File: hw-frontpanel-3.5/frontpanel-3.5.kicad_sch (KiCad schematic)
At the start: 34 parts, among them J1 FRONT_PANEL, J2 QWIIC, J3 Conn_01x02_Pin, J5 OLED_SH1107, J6 Conn_01x12_MountingPin, SW1 SW_Push, SW2 SW_Push, SW3 SW_Push, SW4 SW_Push, U1 MT3540, U2 LM809, U3 TCA9535PWR

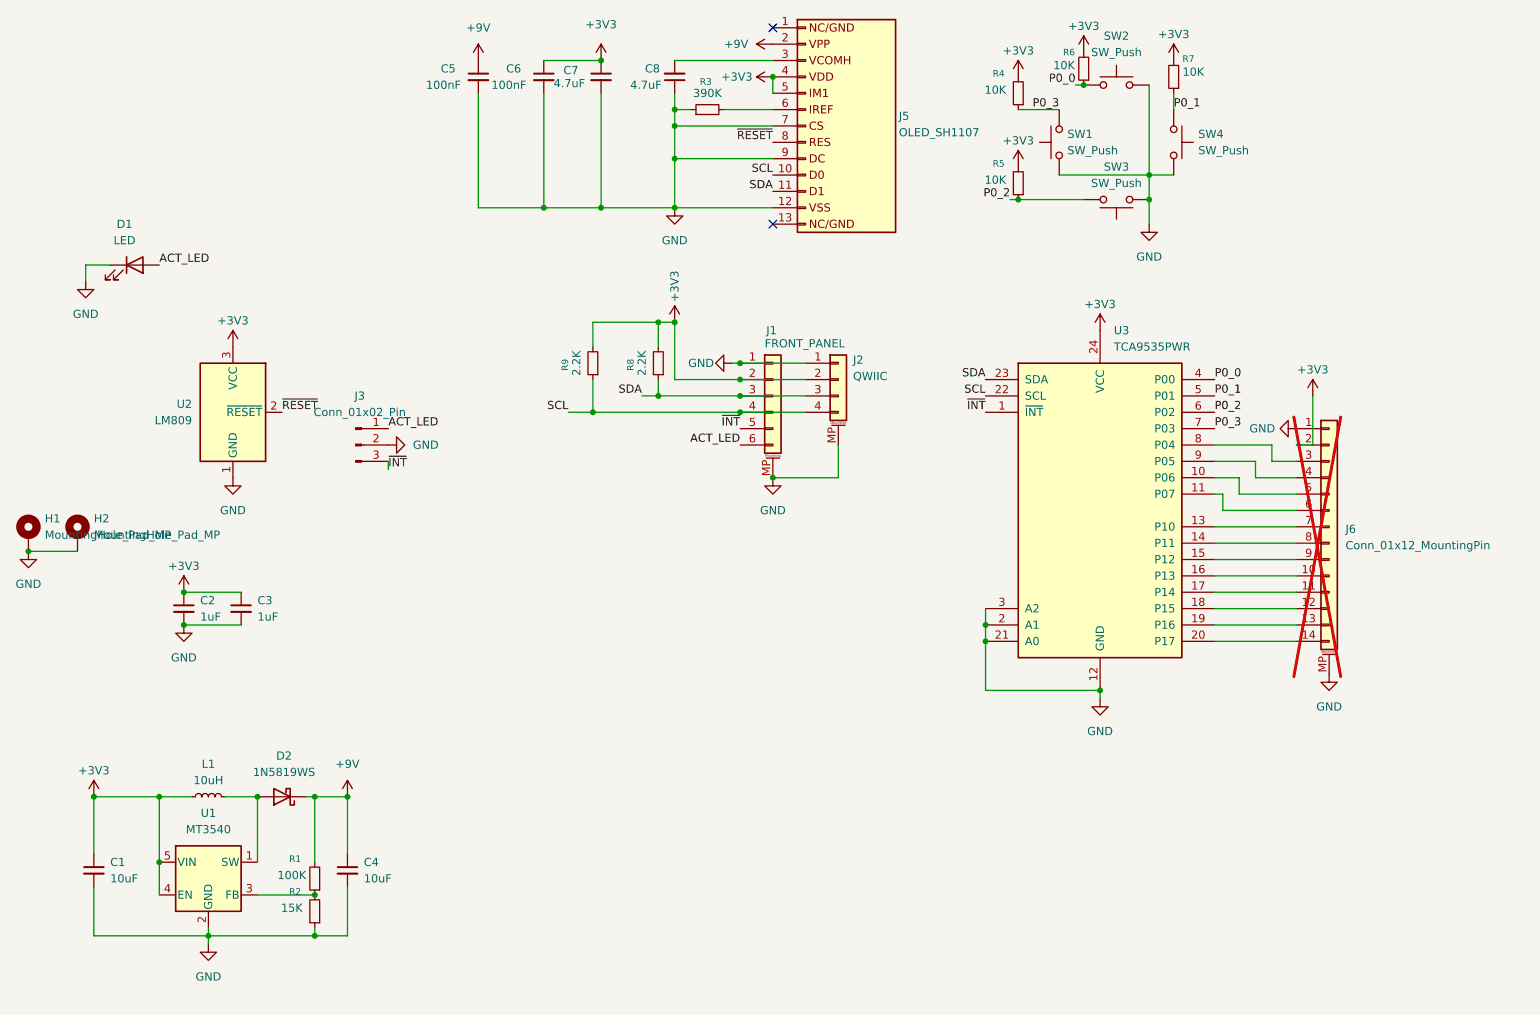
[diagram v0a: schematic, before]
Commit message: Front panel board fabbed at JLCPCB 2025-09-17
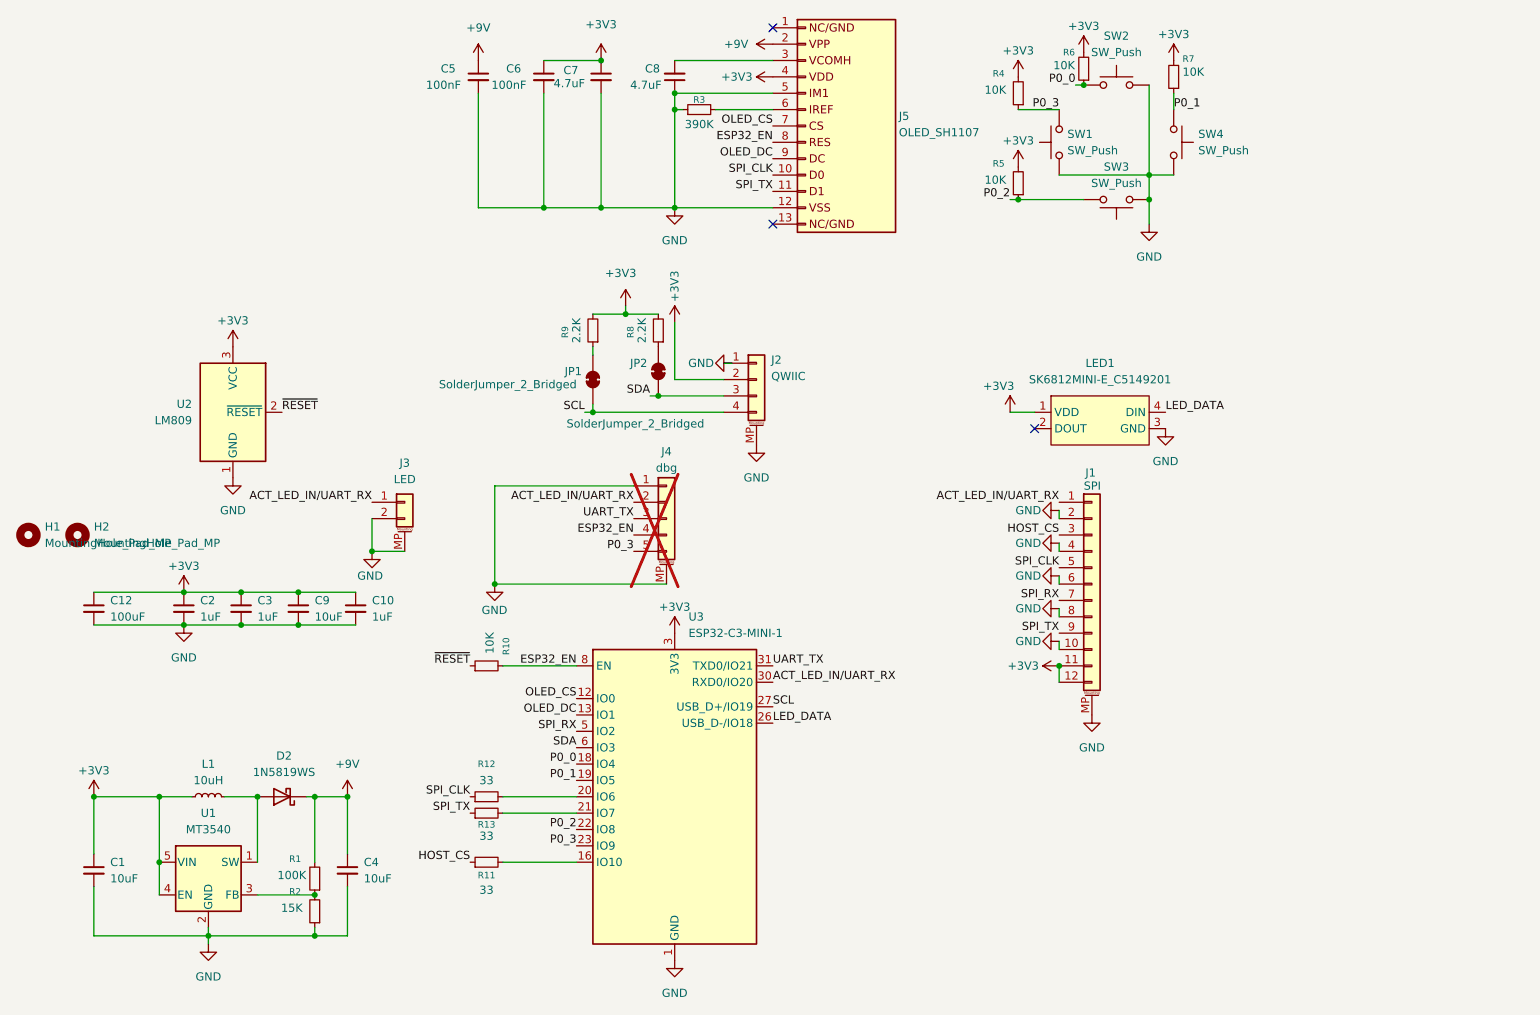
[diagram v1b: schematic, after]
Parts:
- removed D1: LED, LED_SMD:LED_1206_3216Metric_ReverseMount_Hole1.8x2.4mm, symbol Device:LED
- removed J6: Conn_01x12_MountingPin, Connector_JST:JST_SH_BM14B-SRSS-TB_1x14-1MP_P1.00mm_Vertical, symbol Connector_Generic_MountingPin:Conn_01x14_MountingPin
- removed U3: TCA9535PWR, Package_SO:TSSOP-24_4.4x7.8mm_P0.65mm, symbol Interface_Expansion:TCA9535PWR
- added C10: 1uF, Capacitor_SMD:C_0402_1005Metric, symbol Device:C_Small
- added C12: 100uF, Capacitor_SMD:C_1206_3216Metric, symbol Device:C_Small
- added C9: 10uF, Capacitor_SMD:C_0603_1608Metric, symbol Device:C_Small
- added J4: dbg, Connector_JST:JST_SH_BM05B-SRSS-TB_1x05-1MP_P1.00mm_Vertical, symbol Connector_Generic_MountingPin:Conn_01x05_MountingPin
- added JP1, JP2: SolderJumper_2_Bridged, Jumper:SolderJumper-2_P1.3mm_Bridged_RoundedPad1.0x1.5mm, symbol Jumper:SolderJumper_2_Bridged
- added LED1: SK6812MINI-E_C5149201, frontpanel:LED-SMD_L3.2-W2.8-LS5.9_SK6812MINI-E, symbol frontpanel:SK6812MINI-E_C5149201
- added R10: 10K, Resistor_SMD:R_0402_1005Metric, symbol Device:R_Small
- added R11, R12, R13: 33, Resistor_SMD:R_0402_1005Metric, symbol Device:R_Small
- added U3: ESP32-C3-MINI-1, RF_Module:ESP32-C6-MINI-1, symbol frontpanel:ESP32-C3-MINI-1
- C2, C3, C5, C6: footprint Capacitor_SMD:C_0603_1608Metric -> Capacitor_SMD:C_0402_1005Metric
- H1, H2: footprint MountingHole:MountingHole_2.2mm_M2_Pad -> MountingHole:MountingHole_2.2mm_M2; symbol Mechanical:MountingHole_Pad -> Mechanical:MountingHole
- J1: value FRONT_PANEL -> SPI; footprint Connector_JST:JST_SH_BM06B-SRSS-TB_1x06-1MP_P1.00mm_Vertical -> frontpanel:FPC-SMD_12P-L11.5-W2.0-P0.50; symbol Connector_Generic_MountingPin:Conn_01x06_MountingPin -> Connector_Generic_MountingPin:Conn_01x12_MountingPin
- J3: value Conn_01x02_Pin -> LED; footprint Connector_PinHeader_2.54mm:PinHeader_1x03_P2.54mm_Vertical_SMD_Pin1Left -> Connector_JST:JST_SH_BM02B-SRSS-TB_1x02-1MP_P1.00mm_Vertical; symbol Connector:Conn_01x03_Pin -> Connector_Generic_MountingPin:Conn_01x02_MountingPin
- R1, R2, R3, R4, R5, R6, R7, R8, R9: footprint Resistor_SMD:R_0603_1608Metric -> Resistor_SMD:R_0402_1005Metric
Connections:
- net +3V3: now also J1.11 (Pin_11), J1.12 (Pin_12), C10.1, C12.1, C9.1, LED1.1 (VDD), U3.3 (3V3); no longer J1.2 (Pin_2), J5.5 (Pin_5)
- net GND: now also J1.10 (Pin_10), J1.2 (Pin_2), J1.4 (Pin_4), J1.6 (Pin_6), J1.8 (Pin_8), J3.MP (MountPin), J5.5 (Pin_5), C10.2, C12.2, C9.2, J4.1 (Pin_1), J4.MP (MountPin), LED1.3 (GND), U3.1 (GND), U3.11 (GND), U3.14 (GND), U3.2 (GND), U3.36 (GND), U3.37 (GND), U3.38 (GND), U3.39 (GND), U3.40 (GND), U3.41 (GND), U3.42 (GND), U3.43 (GND), U3.44 (GND), U3.45 (GND), U3.46 (GND), U3.47 (GND), U3.48 (GND), U3.49 (GND), U3.50 (GND), U3.51 (GND), U3.52 (GND), U3.53 (GND); no longer H1.1, H2.1, J1.1 (Pin_1), J5.7 (Pin_7), J5.9 (Pin_9)
- net P0_0: now also U3.18 (IO4)
- net P0_1: now also U3.19 (IO5)
- net P0_2: now also U3.22 (IO8)
- net P0_3: now also J4.5 (Pin_5), U3.23 (IO9)
- net SCL: now also JP1.1 (A), U3.27 (USB_D+/IO19); no longer J1.4 (Pin_4), J5.10 (Pin_10), R9.1
- net SDA: now also JP2.1 (A), U3.6 (IO3); no longer J1.3 (Pin_3), J5.11 (Pin_11), R8.1
- net ~{RESET}: now also R10.1; no longer J5.8 (Pin_8)
- net ACT_LED renamed ACT_LED_IN/UART_RX
- net ACT_LED_IN/UART_RX: now also J1.1 (Pin_1), J4.2 (Pin_2), U3.30 (RXD0/IO20); no longer J1.6 (Pin_6)
- net ~{INT} renamed SPI_CLK
- net SPI_CLK: now also J5.10 (Pin_10), R12.1; no longer J3.3 (Pin_3)
- new net: JP1.2 (B), R9.1
- new net: JP2.2 (B), R8.1
- new net: R11.2, U3.16 (IO10)
- new net: R13.2, U3.21 (IO7)
- new net: R12.2, U3.20 (IO6)
- new net ESP32_EN: J4.4 (Pin_4), J5.8 (Pin_8), R10.2, U3.8 (EN)
- new net HOST_CS: J1.3 (Pin_3), R11.1
- new net LED_DATA: LED1.4 (DIN), U3.26 (USB_D-/IO18)
- new net OLED_CS: J5.7 (Pin_7), U3.12 (IO0)
- new net OLED_DC: J5.9 (Pin_9), U3.13 (IO1)
- new net SPI_RX: J1.7 (Pin_7), U3.5 (IO2)
- new net SPI_TX: J1.9 (Pin_9), J5.11 (Pin_11), R13.1
- new net UART_TX: J4.3 (Pin_3), U3.31 (TXD0/IO21)
- no-connect marks 2 -> 3
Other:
- moved on the sheet: J2, R3, R8, R9

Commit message: Use RC for ESP32 reset, power on reset for OLED
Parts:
- added C11: 1uF, Capacitor_SMD:C_0402_1005Metric, symbol Device:C_Small
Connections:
- net +3V3: now also R10.2
- net ESP32_EN: now also R10.1, C11.1; no longer J5.8 (Pin_8), R10.2
- net GND: now also C11.2
- net ~{RESET}: now also J5.8 (Pin_8); no longer R10.1
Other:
- moved on the sheet: J4, R10

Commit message: Provisional v1.0.0 hardware
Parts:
- removed J4: dbg, Connector_JST:JST_SH_BM05B-SRSS-TB_1x05-1MP_P1.00mm_Vertical, symbol Connector_Generic_MountingPin:Conn_01x05_MountingPin
- added J4: TC2030, Connector:Tag-Connect_TC2030-IDC-NL_2x03_P1.27mm_Vertical, symbol Connector:TC2030
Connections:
- net +3V3: now also J4.2
- net ACT_LED_IN/UART_RX: now also J4.5
- net ESP32_EN: now also J4.1
- net GND: now also J4.4
- net P0_3: now also J4.6
- net UART_TX: now also J4.3
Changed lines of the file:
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@@
 	)
 	(junction
-		(at 92.71 115.57)
-		(diameter 0)
-		(color 0 0 0 0)
-	)
-	(junction
 		(at 60.96 170.18)
 		(diameter 0)
@@
 	(wire
 		(pts
-			(xy 92.71 115.57) (xy 119.38 115.57)
-		)
-		(stroke
-			(width 0)
-			(type default)
-		)
-	)
-	(wire
-		(pts
 			(xy 116.84 34.29) (xy 132.08 34.29)
 		)
@@
 	(wire
 		(pts
-			(xy 92.71 100.33) (xy 114.3 100.33)
-		)
-		(stroke
-			(width 0)
-			(type default)
-		)
-	)
-	(wire
-		(pts
 			(xy 116.84 39.37) (xy 132.08 39.37)
 		)
@@
 	(wire
 		(pts
-			(xy 92.71 100.33) (xy 92.71 115.57)
+			(xy 144.78 104.14) (xy 144.78 105.41)
 		)
 		(stroke
@@
 	(wire
 		(pts
+			(xy 144.78 106.68) (xy 144.78 107.95)
+		)
+		(stroke
+			(width 0)
+			(type default)
+		)
+	)
+	(wire
+		(pts
 			(xy 168.91 88.9) (xy 172.72 88.9)
 		)
@@
 	)
 	(label "ACT_LED_IN{slash}UART_RX"
-		(at 114.3 102.87 180)
+		(at 132.08 110.49 180)
 		(effects
 			(font
@@
 	)
 	(label "P0_3"
-		(at 114.3 110.49 180)
+		(at 144.78 110.49 0)
 		(effects
 			(font
 				(size 1.27 1.27)
 			)
-			(justify right bottom)
+			(justify left bottom)
 		)
 	)
@@
 	)
 	(label "UART_TX"
-		(at 114.3 105.41 180)
+		(at 132.08 107.95 180)
 		(effects
 			(font
@@
 	)
 	(label "ESP32_EN"
-		(at 114.3 107.95 180)
+		(at 132.08 105.41 180)
 		(effects
 			(font
@@
 	)
 	(symbol
-		(lib_id "Connector_Generic_MountingPin:Conn_01x05_MountingPin")
-		(at 119.38 105.41 0)
-		(unit 1)
-		(exclude_from_sim no)
-		(in_bom yes)
-		(on_board yes)
-		(dnp yes)
-		(property "Reference" "J4"
-			(at 119.38 94.996 0)
-			(effects
-				(font
-					(size 1.27 1.27)
-				)
-			)
-		)
-		(property "Value" "dbg"
-			(at 119.38 97.536 0)
-			(effects
-				(font
-					(size 1.27 1.27)
-				)
-			)
-		)
-		(property "Footprint" "Connector_JST:JST_SH_BM05B-SRSS-TB_1x05-1MP_P1.00mm_Vertical"
-			(at 119.38 105.41 0)
-			(effects
-				(font
-					(size 1.27 1.27)
-				)
-				(hide yes)
-			)
-		)
-		(property "Datasheet" "~"
-			(at 119.38 105.41 0)
-			(effects
-				(font
-					(size 1.27 1.27)
-				)
-				(hide yes)
-			)
-		)
-		(property "Description" "Generic connectable mounting pin connector, single row, 01x05, script generated (kicad-library-utils/schlib/autogen/connector/)"
-			(at 119.38 105.41 0)
-			(effects
-				(font
-					(size 1.27 1.27)
-				)
-				(hide yes)
-			)
-		)
-		(property "LCSC" "C22438427"
-			(at 119.38 105.41 0)
-			(effects
-				(font
-					(size 1.27 1.27)
-				)
-				(hide yes)
-			)
-		)
-		(pin "2"
-		)
-		(pin "1"
-		)
-		(pin "3"
-		)
-		(pin "MP"
-		)
-		(pin "5"
-		)
-		(pin "4"
-		)
-		(instances
-			(project "frontpanel-3.5"
-				(path "/c6faebfb-76d3-4c2f-8f32-d834e013b78c"
-					(reference "J4")
-					(unit 1)
-				)
-			)
-		)
-	)
-	(symbol
 		(lib_id "Device:R_Small")
 		(at 87.63 151.13 90)
@@
 	)
 	(symbol
+		(lib_id "power:+3V3")
+		(at 144.78 104.14 270)
+		(unit 1)
+		(exclude_from_sim no)
+		(in_bom yes)
+		(on_board yes)
+		(dnp no)
+		(property "Reference" "#PWR037"
+			(at 140.97 104.14 0)
+			(effects
+				(font
+					(size 1.27 1.27)
+				)
+				(hide yes)
+			)
+		)
+		(property "Value" "+3V3"
+			(at 150.114 104.14 90)
+			(effects
+				(font
+					(size 1.27 1.27)
+				)
+			)
+		)
+		(property "Footprint" ""
+			(at 144.78 104.14 0)
+			(effects
+				(font
+					(size 1.27 1.27)
+				)
+				(hide yes)
+			)
+		)
+		(property "Datasheet" ""
+			(at 144.78 104.14 0)
+			(effects
+				(font
+					(size 1.27 1.27)
+				)
+				(hide yes)
+			)
+		)
+		(property "Description" "Power symbol creates a global label with name \"+3V3\""
+			(at 144.78 104.14 0)
+			(effects
+				(font
+					(size 1.27 1.27)
+				)
+				(hide yes)
+			)
+		)
+		(pin "1"
+		)
+		(instances
+			(project "frontpanel-3.5"
+				(path "/c6faebfb-76d3-4c2f-8f32-d834e013b78c"
+					(reference "#PWR037")
+					(unit 1)
+				)
+			)
+		)
+	)
+	(symbol
 		(lib_id "Device:C_Small")
 		(at 96.52 36.83 0)
@@
 	(symbol
 		(lib_id "power:GND")
-		(at 92.71 115.57 0)
-		(unit 1)
-		(exclude_from_sim no)
-		(in_bom yes)
-		(on_board yes)
-		(dnp no)
-		(property "Reference" "#PWR02"
-			(at 92.71 121.92 0)
-			(effects
-				(font
-					(size 1.27 1.27)
-				)
-				(hide yes)
-			)
-		)
-		(property "Value" "GND"
-			(at 90.678 119.634 0)
-			(effects
-				(font
-					(size 1.27 1.27)
-				)
-				(justify left)
-			)
-		)
-		(property "Footprint" ""
-			(at 92.71 115.57 0)
-			(effects
-				(font
-					(size 1.27 1.27)
-				)
-				(hide yes)
-			)
-		)
-		(property "Datasheet" ""
-			(at 92.71 115.57 0)
-			(effects
-				(font
-					(size 1.27 1.27)
-				)
-				(hide yes)
-			)
-		)
-		(property "Description" "Power symbol creates a global label with name \"GND\" , ground"
-			(at 92.71 115.57 0)
-			(effects
-				(font
-					(size 1.27 1.27)
-				)
-				(hide yes)
-			)
-		)
-		(pin "1"
-		)
-		(instances
-			(project "frontpanel-3.5"
-				(path "/c6faebfb-76d3-4c2f-8f32-d834e013b78c"
-					(reference "#PWR02")
-					(unit 1)
-				)
-			)
-		)
-	)
-	(symbol
-		(lib_id "power:GND")
 		(at 176.53 124.46 270)
 		(unit 1)
@@
 	)
 	(symbol
+		(lib_id "power:GND")
+		(at 144.78 106.68 90)
+		(unit 1)
+		(exclude_from_sim no)
+		(in_bom yes)
+		(on_board yes)
+		(dnp no)
+		(fields_autoplaced yes)
+		(property "Reference" "#PWR038"
+			(at 151.13 106.68 0)
+			(effects
+				(font
+					(size 1.27 1.27)
+				)
+				(hide yes)
+			)
+		)
+		(property "Value" "GND"
+			(at 148.59 106.6799 90)
+			(effects
+				(font
+					(size 1.27 1.27)
+				)
+				(justify right)
+			)
+		)
+		(property "Footprint" ""
+			(at 144.78 106.68 0)
+			(effects
+				(font
+					(size 1.27 1.27)
+				)
+				(hide yes)
+			)
+		)
+		(property "Datasheet" ""
+			(at 144.78 106.68 0)
+			(effects
+				(font
+					(size 1.27 1.27)
+				)
+				(hide yes)
+			)
+		)
+		(property "Description" "Power symbol creates a global label with name \"GND\" , ground"
+			(at 144.78 106.68 0)
+			(effects
+				(font
+					(size 1.27 1.27)
+				)
+				(hide yes)
+			)
+		)
+		(pin "1"
+		)
+		(instances
+			(project "frontpanel-3.5"
+				(path "/c6faebfb-76d3-4c2f-8f32-d834e013b78c"
+					(reference "#PWR038")
+					(unit 1)
+				)
+			)
+		)
+	)
+	(symbol
 		(lib_id "Device:C_Small")
 		(at 26.67 119.38 0)
@@
 					(unit 1)
 				)
+			)
+		)
+	)
+	(symbol
+		(lib_id "Connector:TC2030")
+		(at 137.16 107.95 0)
+		(unit 1)
+		(exclude_from_sim no)
+		(in_bom no)
+		(on_board yes)
+		(dnp no)
+		(fields_autoplaced yes)
+		(property "Reference" "J4"
+			(at 138.43 95.25 0)
+			(effects
+				(font
+					(size 1.27 1.27)
+				)
+			)
+		)
+		(property "Value" "TC2030"
+			(at 138.43 97.79 0)
+			(effects
+				(font
+					(size 1.27 1.27)
+				)
+			)
+		)
+		(property "Footprint" "Connector:Tag-Connect_TC2030-IDC-NL_2x03_P1.27mm_Vertical"
+			(at 138.43 107.95 0)
+			(effects
+				(font
+					(size 1.27 1.27)
+				)
+				(hide yes)
+			)
+		)
+		(property "Datasheet" "https://www.tag-connect.com/wp-content/uploads/bsk-pdf-manager/2019/12/TC2030-IDC-NL-Datasheet-Rev-B.pdf"
+			(at 138.43 107.95 0)
+			(effects
+				(font
+					(size 1.27 1.27)
+				)
+				(hide yes)
+			)
+		)
+		(property "Description" "Tag-Connect’s 6-pins connector"
+			(at 137.16 107.95 0)
+			(effects
+				(font
+					(size 1.27 1.27)
+				)
+				(hide yes)
+			)
+		)
+		(pin "1"
+		)
+		(pin "3"
+		)
+		(pin "4"
+		)
+		(pin "5"
+		)
+		(pin "2"
+		)
+		(pin "6"
+		)
+		(instances
+			(project ""
+				(path "/c6faebfb-76d3-4c2f-8f32-d834e013b78c"
+					(reference "J4")
+					(unit 1)
+				)

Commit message: Final v1.0.0 front panel design
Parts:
- added J6: dbg, Connector_JST:JST_SH_BM05B-SRSS-TB_1x05-1MP_P1.00mm_Vertical, symbol Connector_Generic_MountingPin:Conn_01x05_MountingPin
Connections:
- net ACT_LED_IN/UART_RX: now also J6.2 (Pin_2)
- net ESP32_EN: now also J6.4 (Pin_4)
- net GND: now also J6.1 (Pin_1), J6.MP (MountPin)
- net P0_3: now also J6.5 (Pin_5)
- net UART_TX: now also J6.3 (Pin_3)
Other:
- moved on the sheet: C1, C10, C12, C2, C3, C4, C9, D2, H1, H2, J3, L1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
